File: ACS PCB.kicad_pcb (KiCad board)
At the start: 4 copper layers, 72.4 x 72.4 mm, 72 parts, among them J1 Conn_01x02, J3 Conn_01x01, J5 Conn_01x02, Q1 2SC1815, U1 LSM6DSV80XTR, U3 LSM6DSV80XTR, U4 BMP581, U5 BMP581, U6 BMP581, U7 LSM6DSV80XTR, U8 PLM62440APPQRJRTQ1

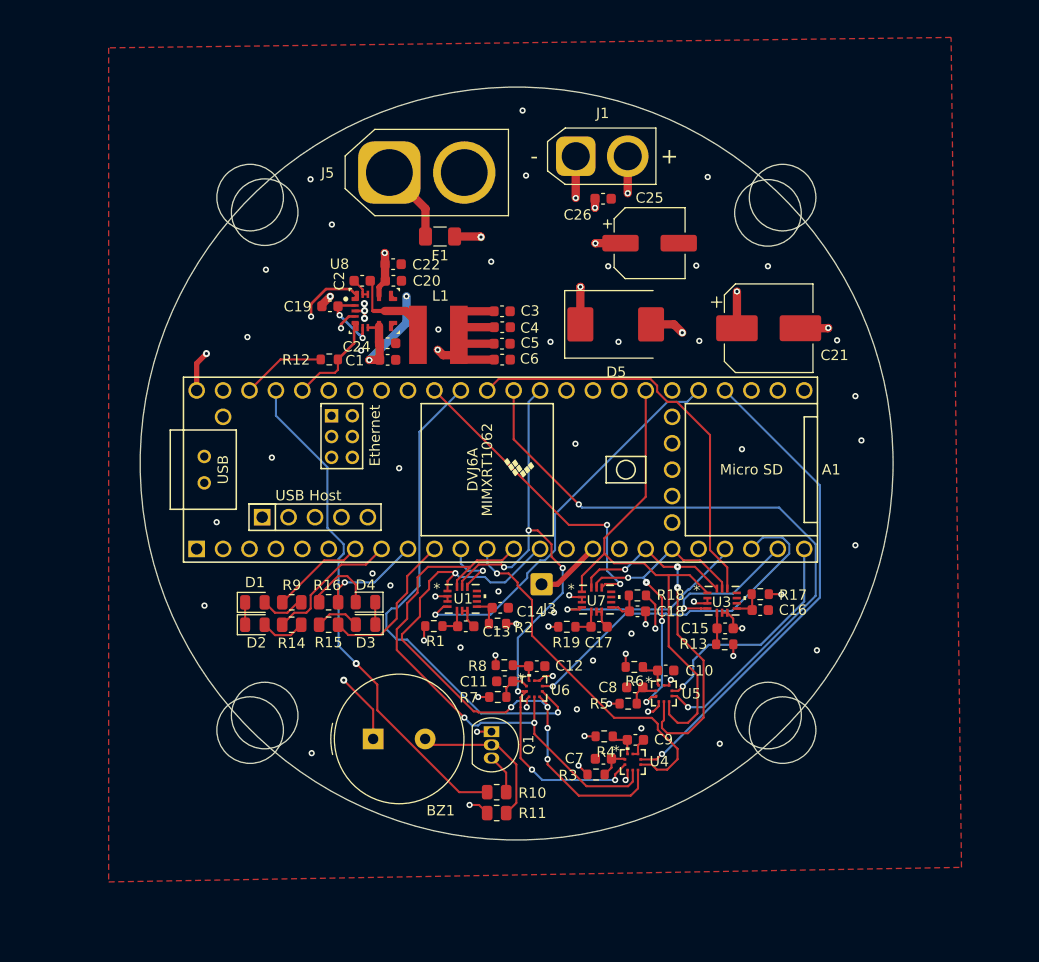
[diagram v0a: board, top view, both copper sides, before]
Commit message: Redid Footprints/Picked components
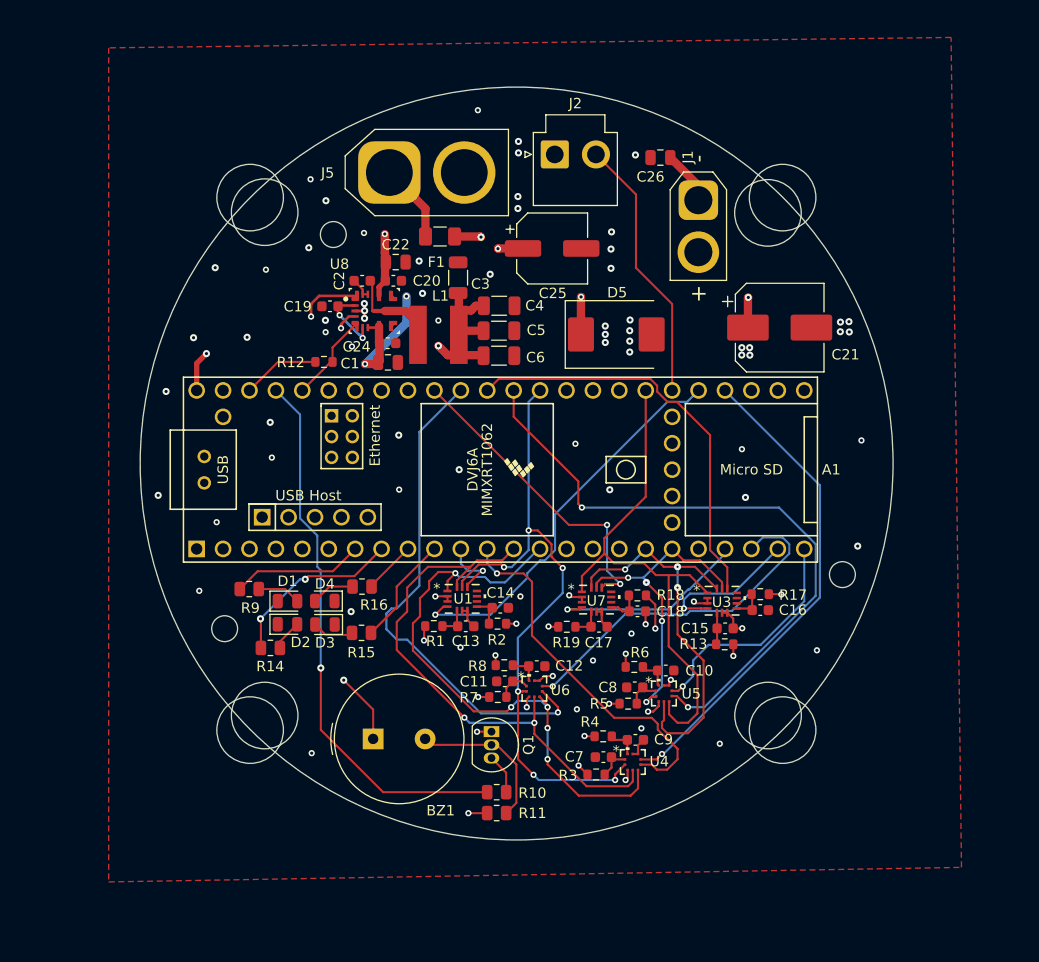
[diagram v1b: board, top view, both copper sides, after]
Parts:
- removed J3: Conn_01x01, Connector_Wire:SolderWire-0.5sqmm_1x01_D0.9mm_OD2.1mm
- added J2: Conn_01x02_Socket, Connector_JST:JST_VH_B2P-VH-B_1x02_P3.96mm_Vertical, F.Cu at (151.7, 57.9)
- C1, C22: value 10uF -> 10u; footprint Capacitor_SMD:C_0603_1608Metric -> Capacitor_SMD:C_0805_2012Metric
- C19: value 1uF -> 1u
- C2, C20, C24: value 100nF -> 100n
- C21: value 100uF -> 100u
- C26: value 1uF -> 1u; footprint Capacitor_SMD:C_0603_1608Metric -> Capacitor_SMD:C_0805_2012Metric
- C3, C4, C5, C6: value 22uF -> 22u; footprint Capacitor_SMD:C_0603_1608Metric -> Capacitor_SMD:C_1206_3216Metric
- R14, R15, R16, R9: value 1K -> 1k
- U8: value PLM62440APPQRJRTQ1 -> LM62440CLPQRJRRQ1
- moved J1 12.5 mm to (165.5, 62.2), turned to -90 degrees
- moved C25 9.38 mm to (151.4, 66.9)
- moved C26 6.79 mm to (161.8, 58.1), turned to 180 degrees
- moved C3 5.32 mm to (142.4, 69.7), turned to 90 degrees
- moved R9 4.28 mm to (122.3, 99.6)
- moved D4 3.91 mm to (129.6, 100.8)
- moved D3 3.91 mm to (129.6, 103.0)
- moved R16 3.55 mm to (133.2, 99.4)
- moved R15 3.26 mm to (133.1, 103.8)
- moved D1 3.14 mm to (126.0, 100.8)
- moved D2 3.13 mm to (126.0, 103.0)
- moved R14 3.03 mm to (124.3, 105.3)
- moved C4 2.08 mm to (146.3, 72.4)
- moved C5 1.28 mm to (146.3, 74.8)
- moved C21 1.06 mm to (173.3, 74.5)
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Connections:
- A1 pad 24: PWM_fs -> unconnected-(A1-A10-Pad24)
- A1 pad 38: unconnected-(A1-A14-Pad38) -> PWM
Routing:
- net PWM: track 0.00 -> 25.7 mm
- net GND: track 43.4 -> 26.8 mm, vias 56 -> 67
- net PWM_fs: track 6.35 -> 0.00 mm
- net GREEN_LED: track 9.59 -> 5.07 mm, vias 1 -> 0
- net BLUE_LED: track 14.9 -> 10.6 mm
- net YELLOW_LED: track 13.3 -> 17.2 mm, vias 0 -> 2
- net Buzzer: track 49.0 -> 52.9 mm
- net RED_LED: track 9.13 -> 12.7 mm
- net +BATT: track 34.4 -> 37.9 mm, vias 9 -> 11
- net Net-(D4-A): track 7.00 -> 4.18 mm
- net +5V: track 36.2 -> 34.8 mm, vias 4 -> 5
- net Net-(D2-A): track 4.34 -> 2.96 mm
- net MISO0: track 57.9 -> 57.0 mm
- net CS_A0: track 34.8 -> 35.6 mm
- net +3.3V: track 32.8 -> 32.0 mm, vias 14 -> 20
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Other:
- outline, holes or cut-outs redrawn

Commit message: finalized
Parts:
- removed J1: Conn_01x02, Connector_AMASS:AMASS_XT30U-F_1x02_P5.0mm_Vertical
- added J3: Conn_01x02, Connector_AMASS:AMASS_XT30U-F_1x02_P5.0mm_Vertical, F.Cu at (165.4, 62.3)
- moved C26 14.7 mm to (165.2, 72.5), turned to -90 degrees
- moved D5 0.76 mm to (156.8, 75.1)
- moved C21 0.50 mm to (173.3, 74.0)
- moved C1 0.30 mm to (135.7, 77.5)
- moved C24 0.25 mm to (135.6, 75.8)
- moved C25 0.21 mm to (151.7, 66.9)
- moved F1 0.06 mm to (140.6, 65.8)
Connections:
- F1 pad 1: +BATT -> Net-(J5-Pin_2)
- F1 pad 2: Net-(J5-Pin_1) -> +BATT
- J5 pad 1: Net-(J5-Pin_1) -> GND
- J5 pad 2: GND -> Net-(J5-Pin_2)
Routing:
- net Net-(J5-Pin_1): track 7.59 -> 0.00 mm
- net Net-(J5-Pin_2): track 0.00 -> 6.54 mm
- net CS_I1: track 39.9 -> 38.0 mm, vias 0 -> 2
- net +BATT: track 37.9 -> 39.6 mm, vias 11 -> 12
- net GND: vias 67 -> 71

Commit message: Almost Final Revisions
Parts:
- moved C9 33.6 mm to (128.7, 100.6), turned to -90 degrees
- moved U4 32.2 mm to (130.9, 100.9), turned to 90 degrees
- moved R4 29.7 mm to (128.4, 103.7), turned to -90 degrees
- moved C7 28.7 mm to (130.4, 103.7), turned to -90 degrees
- moved R3 27.0 mm to (132.1, 104.4), turned to -90 degrees
- moved R15 9.55 mm to (123.8, 106.0)
- moved R16 9.33 mm to (123.8, 99.0)
- moved R6 8.39 mm to (165.6, 112.8), turned to 0 degrees
- moved R5 7.52 mm to (166.1, 109.2), turned to 0 degrees
- moved C8 6.36 mm to (165.5, 110.8), turned to 0 degrees
- moved R18 6.33 mm to (154.3, 103.7), turned to 180 degrees
- moved D2 6.32 mm to (119.7, 103.8)
- moved D1 6.29 mm to (119.7, 101.1)
- moved D3 5.77 mm to (123.9, 103.8)
- moved D4 5.74 mm to (123.9, 101.1)
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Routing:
- net CS_A1: track 61.6 -> 36.2 mm, vias 2 -> 1
- net MOSI0: track 53.2 -> 32.3 mm, vias 2 -> 3
- net CS_A0: track 35.6 -> 17.7 mm, vias 1 -> 2
- net MISO0: track 57.0 -> 45.0 mm, vias 5 -> 3
- net MOSI1: track 38.8 -> 27.0 mm
- net CS_A2: track 48.8 -> 37.9 mm
- net GREEN_LED: track 5.07 -> 15.9 mm, vias 0 -> 1
- net INT_A2: track 34.4 -> 45.0 mm, vias 1 -> 3
- net CS_I2: track 30.1 -> 39.6 mm, vias 2 -> 1
- net BLUE_LED: track 10.6 -> 19.7 mm, vias 0 -> 1
- net SCK0: track 62.7 -> 54.7 mm, vias 6 -> 0
- net GND: track 26.8 -> 19.5 mm, vias 71 -> 131
- net MISO1: track 52.5 -> 46.3 mm, vias 0 -> 3
- net YELLOW_LED: track 17.2 -> 22.5 mm, vias 2 -> 1
- net RED_LED: track 12.7 -> 17.0 mm, vias 0 -> 2
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- added copper zone on B.Cu, net GND
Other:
- outline, holes or cut-outs redrawn

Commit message: Finalized PCB
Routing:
- net INT_A0: track 48.7 -> 49.9 mm
- net CS_A0: track 17.7 -> 18.5 mm
- net MISO0: track 45.0 -> 45.8 mm
- net RED_LED: track 17.0 -> 17.8 mm
- net +3.3V: track 33.7 -> 33.1 mm
- net GREEN_LED: track 15.9 -> 16.4 mm
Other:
- outline, holes or cut-outs redrawn
- board text added: "ACS 2026 - 2027"
- board text added: "HS"
- board text added: "MM"
- board text added: "Margaret Mei Heather Schwartz"
